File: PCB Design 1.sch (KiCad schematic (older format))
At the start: 23 parts, among them Q1 MMBT3906, Q2 MMBT3906, Q3 MMBT3906, Q4 MMBT3906, Q5 MMBT3906, Q6 MMBT3906, Q7 MMBT3906, Q8 MMBT3906, SW1 SW_PUSH, U1 MAX6969, U2 MAX6969

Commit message: Second Commit - TL084's left to implement
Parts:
- added MCU1: MSP430G2353, Housings_DIP:DIP-20_W7.62mm, symbol MSP430G2353
- added R2: 47K, Resistors_SMD:R_0402, symbol R
- added SW2: SW_PUSH, Buttons_Switches_SMD:SW_SPST_EVPBF, symbol SW_PUSH
- added U3: 74HC595, Housings_DIP:DIP-16_W7.62mm, symbol 74HC595
- added U4: CD4051B, Housings_DIP:DIP-16_W7.62mm, symbol 4051
- renumbered MCU1 to MCU2, R4 to R10, R5 to R11, R6 to R12, R7 to R13, R8 to R14, R9 to R15, R10 to R16, R11 to R17, R2 to R3, R3 to R4
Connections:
- net labels added: (A), (B), (C), AnalogInput-(X), CLK, CS, RCLK, SER, SIMO(1)-SOMI(2), SOMI(1)-SIMO(2), SRCLK
- wire segments 56 -> 97
- no-connect marks 46 -> 58
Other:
- note added: "01/27/16"
- note added: "1.0.0"
- note added: "Analog Multiplexer"
- note added: "ELEC 3909 - 3rd Year Project"
- note added: "LED SYNC's"
- note added: "LED Table"
- note added: "Matthew Bovolotto"
- note added: "PNP LED Driver Circuit"
- note added: "Pseudo SPI"
- note added: "Reset Switch"
- note added: "Shift Register (8)"
- moved on the sheet: MCU2, Q1, Q2, Q3, Q4, Q5, Q6, Q7, Q8, R1, R10, R11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

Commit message: UART Tri-State Buffer Update
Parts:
- added U5: 74125/126, Housings_DIP:DIP-14_W7.62mm, symbol 74125
- U3: symbol 74HC595 -> 74HC595-RESCUE-PCB_Design_1
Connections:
- net labels added: UART(CS), UART(RXD), UART(TXD)
- wire segments 97 -> 102
- no-connect marks 58 -> 73
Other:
- note added: "IR LED Driver"
- note added: "LED Matrix Driver"
- note added: "MSP430 - SPI Communication"
- note added: "UART - Bluetooth Module\n (Tri-state Buffer)"
- moved on the sheet: MCU1, MCU2, Q1, Q2, Q3, Q4, Q5, Q6, Q7, Q8, R1, R10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

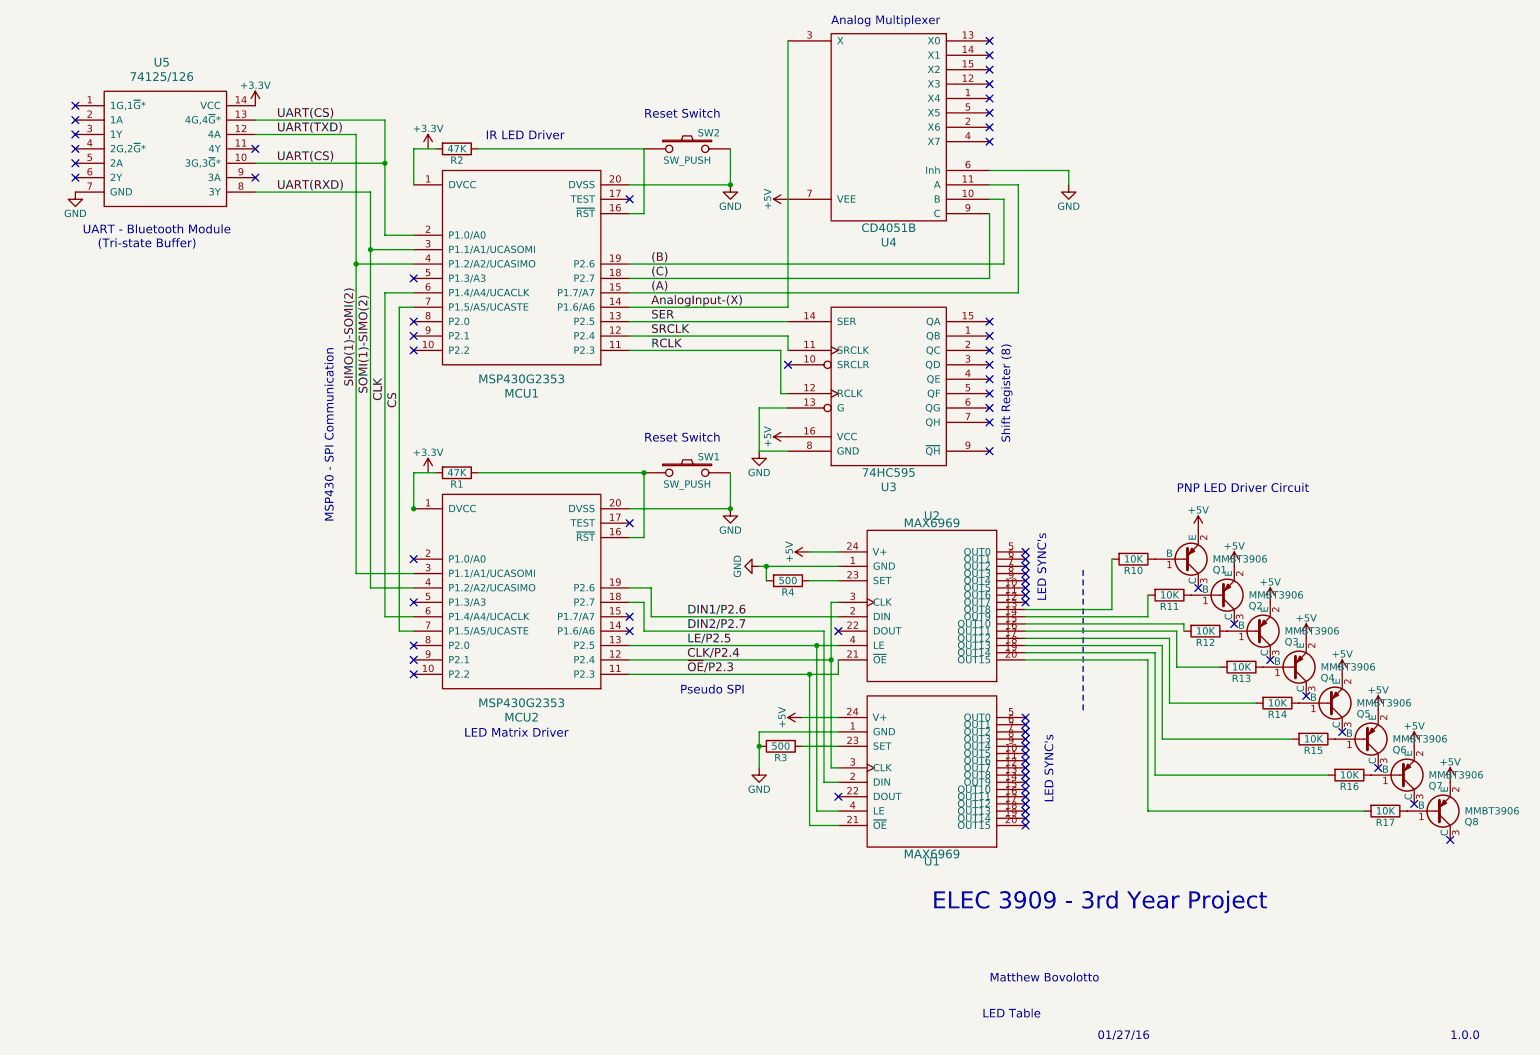
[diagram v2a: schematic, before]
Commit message: OP AMP Buffer Added
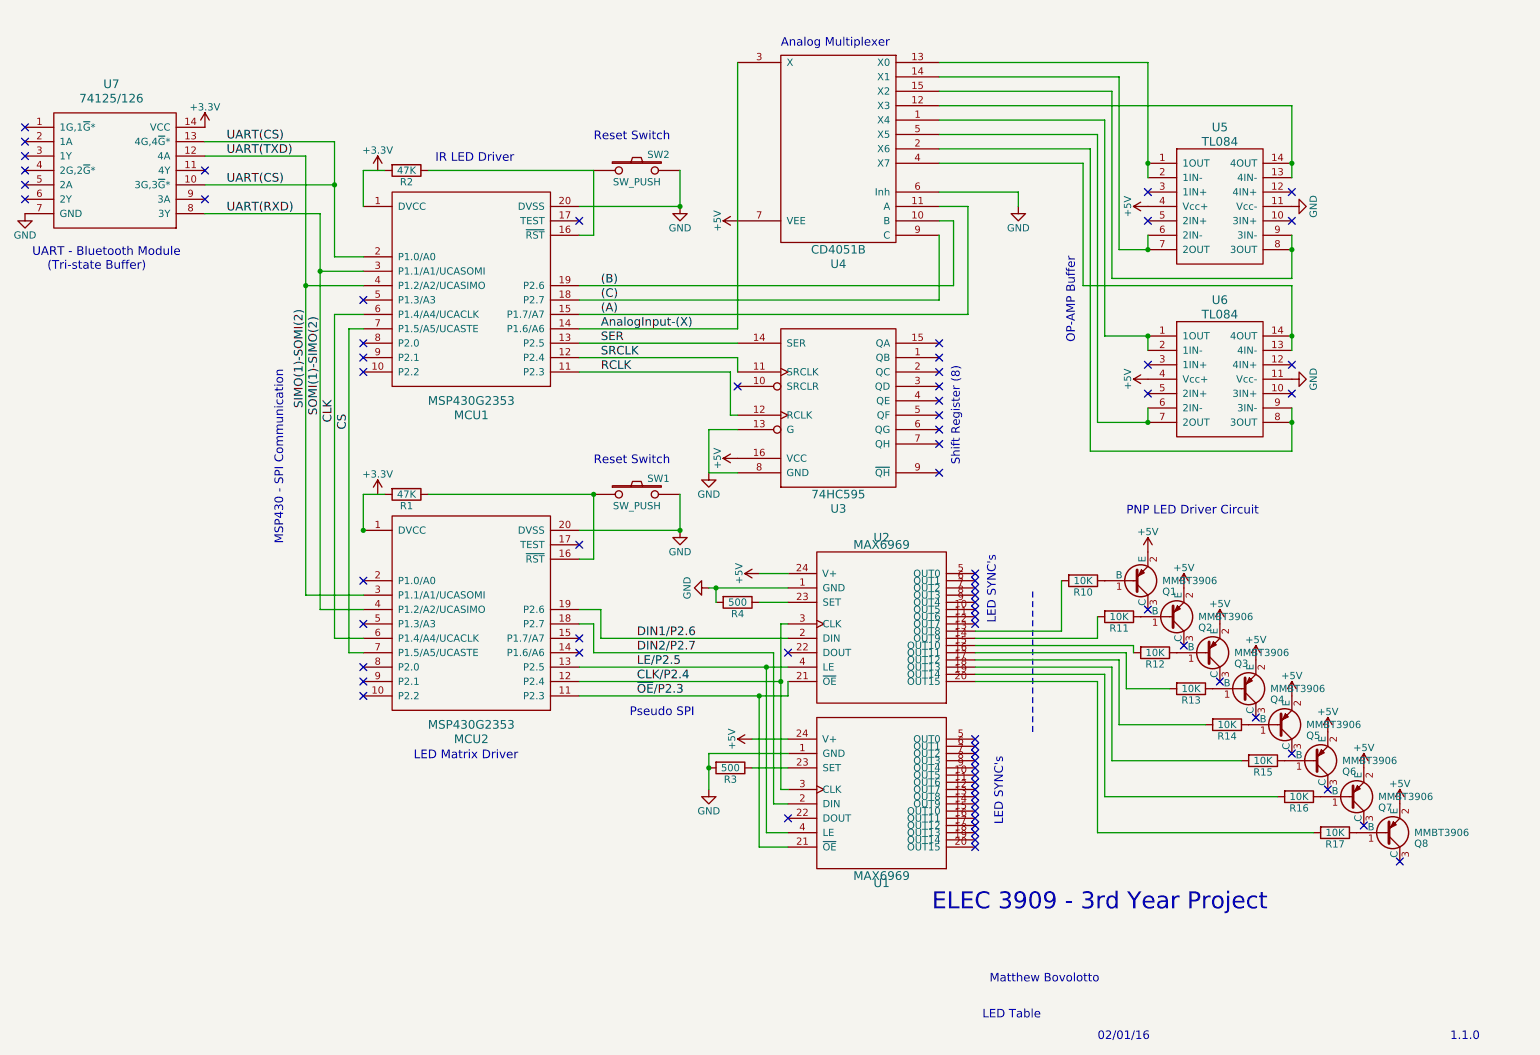
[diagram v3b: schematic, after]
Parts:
- added U5, U6: TL084, Housings_DIP:DIP-14_W7.62mm, symbol TL084
- renumbered U5 to U7
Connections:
- net +5V: now also U5.4 (Vcc+), U6.4 (Vcc+)
- net GND: now also U5.11 (Vcc-), U6.11 (Vcc-)
- net at U4.1 (X4): now also U6.1 (1OUT), U6.2 (1IN-)
- net at U4.12 (X3): now also U5.13 (4IN-), U5.14 (4OUT)
- net at U4.13 (X0): now also U5.1 (1OUT), U5.2 (1IN-)
- net at U4.14 (X1): now also U5.6 (2IN-), U5.7 (2OUT)
- net at U4.15 (X2): now also U5.8 (3OUT), U5.9 (3IN-)
- net at U4.2 (X6): now also U6.8 (3OUT), U6.9 (3IN-)
- net at U4.4 (X7): now also U6.13 (4IN-), U6.14 (4OUT)
- net at U4.5 (X5): now also U6.6 (2IN-), U6.7 (2OUT)
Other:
- note added: "02/01/16"
- note added: "1.1.0"
- note added: "OP-AMP Buffer"
- note removed: "01/27/16"
- note removed: "1.0.0"
- moved on the sheet: MCU1, MCU2, Q1, Q2, Q3, Q4, Q5, Q6, Q7, Q8, R1, R10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

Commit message: Minor Pin Updates
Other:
- note added: "02/05/16"
- note added: "1.1.1"
- note removed: "02/01/16"
- note removed: "1.1.0"
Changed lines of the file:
@@
 L +5V #PWR08
 U 1 1 56A51E9E
-P 9750 5500
-F 0 "#PWR08" H 9750 5350 50  0001 C CNN
-F 1 "+5V" H 9750 5640 50  0000 C CNN
-F 2 "" H 9750 5500 50  0000 C CNN
-F 3 "" H 9750 5500 50  0000 C CNN
-	1    9750 5500
+P 9350 5650
+F 0 "#PWR08" H 9350 5500 50  0001 C CNN
+F 1 "+5V" H 9350 5790 50  0000 C CNN
+F 2 "" H 9350 5650 50  0000 C CNN
+F 3 "" H 9350 5650 50  0000 C CNN
+	1    9350 5650
 	1    0    0    -1
 $EndComp
@@
 L +5V #PWR09
 U 1 1 56A51E8B
-P 10000 5750
-F 0 "#PWR09" H 10000 5600 50  0001 C CNN
-F 1 "+5V" H 10000 5890 50  0000 C CNN
-F 2 "" H 10000 5750 50  0000 C CNN
-F 3 "" H 10000 5750 50  0000 C CNN
-	1    10000 5750
+P 9600 5900
+F 0 "#PWR09" H 9600 5750 50  0001 C CNN
+F 1 "+5V" H 9600 6040 50  0000 C CNN
+F 2 "" H 9600 5900 50  0000 C CNN
+F 3 "" H 9600 5900 50  0000 C CNN
+	1    9600 5900
 	1    0    0    -1
 $EndComp
@@
 ELEC 3909 - 3rd Year Project
 Text Notes 10600 7650 0    59   ~ 0
-1.1.0
+1.1.1
 Text Notes 8150 7650 0    59   ~ 0
-02/01/16
+02/05/16
 Text Notes 7350 7500 0    59   ~ 0
 LED Table
@@
 Text Notes 8000 2800 1    60   ~ 0
 OP-AMP Buffer
+$Comp
+L +5V #PWR027
+U 1 1 56B21263
+P 9750 5500
+F 0 "#PWR027" H 9750 5350 50  0001 C CNN
+F 1 "+5V" H 9750 5640 50  0000 C CNN
+F 2 "" H 9750 5500 50  0000 C CNN
+F 3 "" H 9750 5500 50  0000 C CNN
+	1    9750 5500
+	1    0    0    -1
+$EndComp
+$Comp
+L +5V #PWR028
+U 1 1 56B212CB
+P 10000 5750
+F 0 "#PWR028" H 10000 5600 50  0001 C CNN
+F 1 "+5V" H 10000 5890 50  0000 C CNN
+F 2 "" H 10000 5750 50  0000 C CNN
+F 3 "" H 10000 5750 50  0000 C CNN
+	1    10000 5750
+	1    0    0    -1
+$EndComp
 $EndSCHEMATC

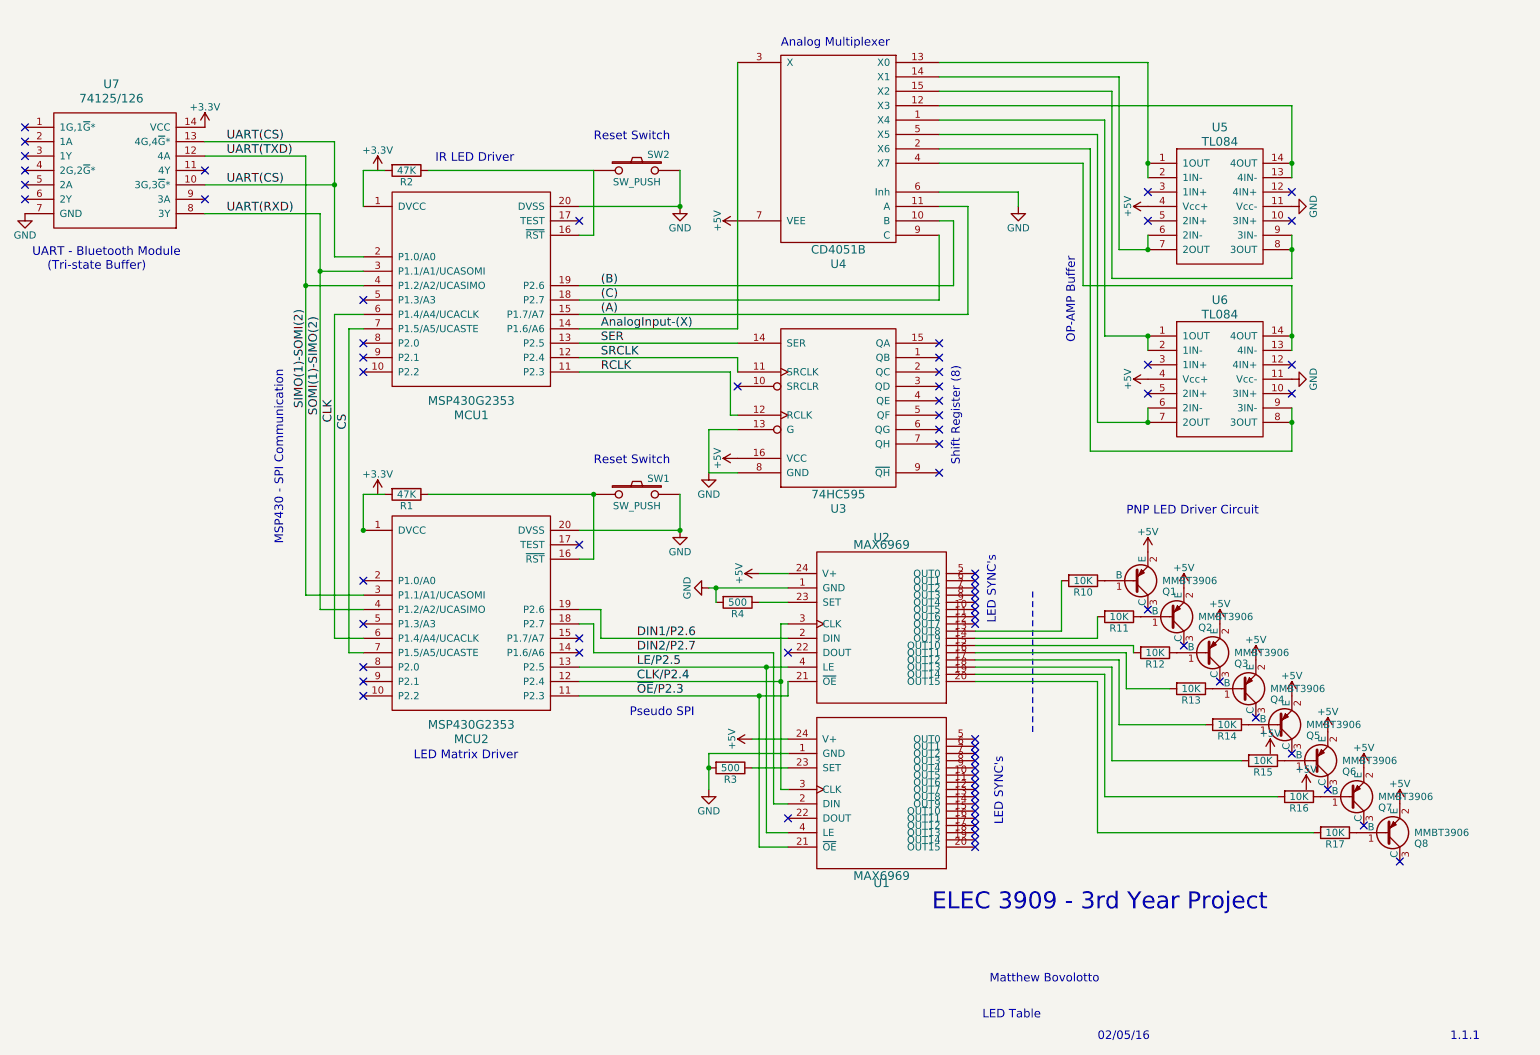
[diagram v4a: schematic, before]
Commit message: IR Led Driver Update
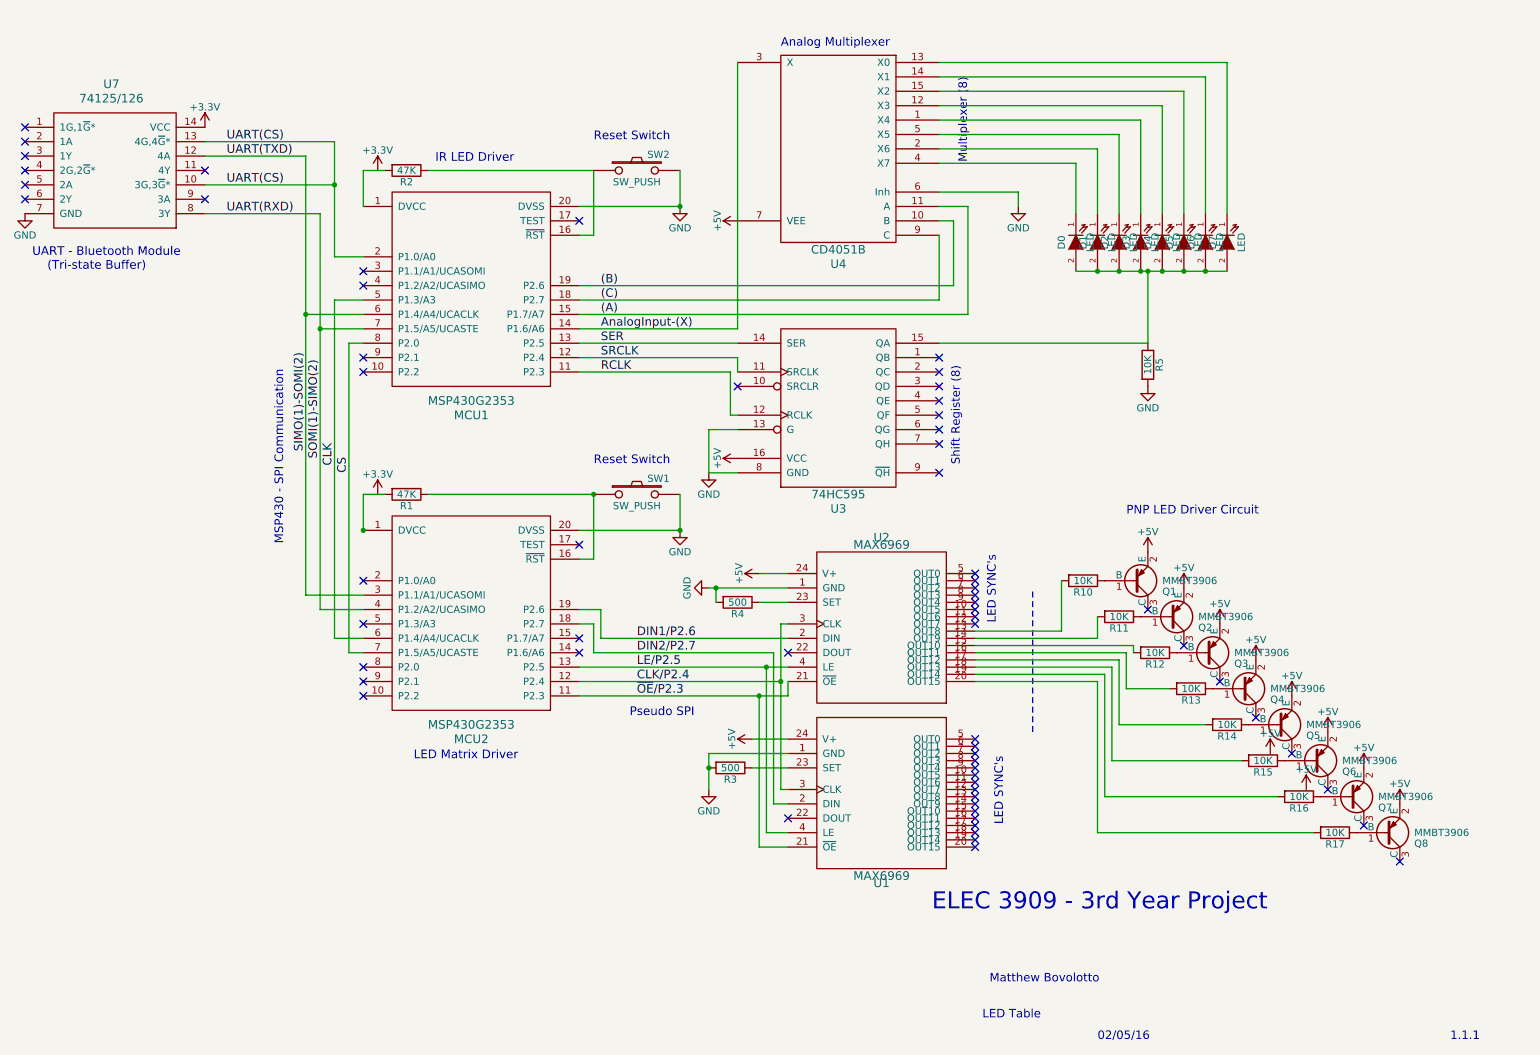
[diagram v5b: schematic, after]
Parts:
- removed U5, U6: TL084, Housings_DIP:DIP-14_W7.62mm, symbol TL084
- added D0, D1, D2, D3, D4, D5, D6, D7: LED, symbol LED
- added R5: 10K, symbol R
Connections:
- net CLK: now also MCU1.5 (P1.3/A3); no longer MCU1.6 (P1.4/A4/UCACLK)
- net CS: now also MCU1.8 (P2.0); no longer MCU1.7 (P1.5/A5/UCASTE)
- net GND: now also R5.2
- net SIMO(1)-SOMI(2): now also MCU1.6 (P1.4/A4/UCACLK); no longer MCU1.4 (P1.2/A2/UCASIMO)
- net SOMI(1)-SIMO(2): now also MCU1.7 (P1.5/A5/UCASTE); no longer MCU1.3 (P1.1/A1/UCASOMI)
- net at U3.15 (QA): now also D0.2 (A), D1.2 (A), D2.2 (A), D3.2 (A), D4.2 (A), D5.2 (A), D6.2 (A), D7.2 (A), R5.1
- net at U4.1 (X4): now also D3.1 (K)
- net at U4.12 (X3): now also D4.1 (K)
- net at U4.13 (X0): now also D7.1 (K)
- net at U4.14 (X1): now also D6.1 (K)
- net at U4.15 (X2): now also D5.1 (K)
- net at U4.2 (X6): now also D1.1 (K)
- net at U4.4 (X7): now also D0.1 (K)
- net at U4.5 (X5): now also D2.1 (K)
- no-connect marks 73 -> 64
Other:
- note added: "Multiplexer (8)"
- note removed: "OP-AMP Buffer"
